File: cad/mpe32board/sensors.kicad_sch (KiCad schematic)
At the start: 93 parts, among them U4 TCA9548ARGER, U5 TCA9548ARGER, U6 TCA9548ARGER, U7 TCA9548ARGER, U8 TCA9548ARGER

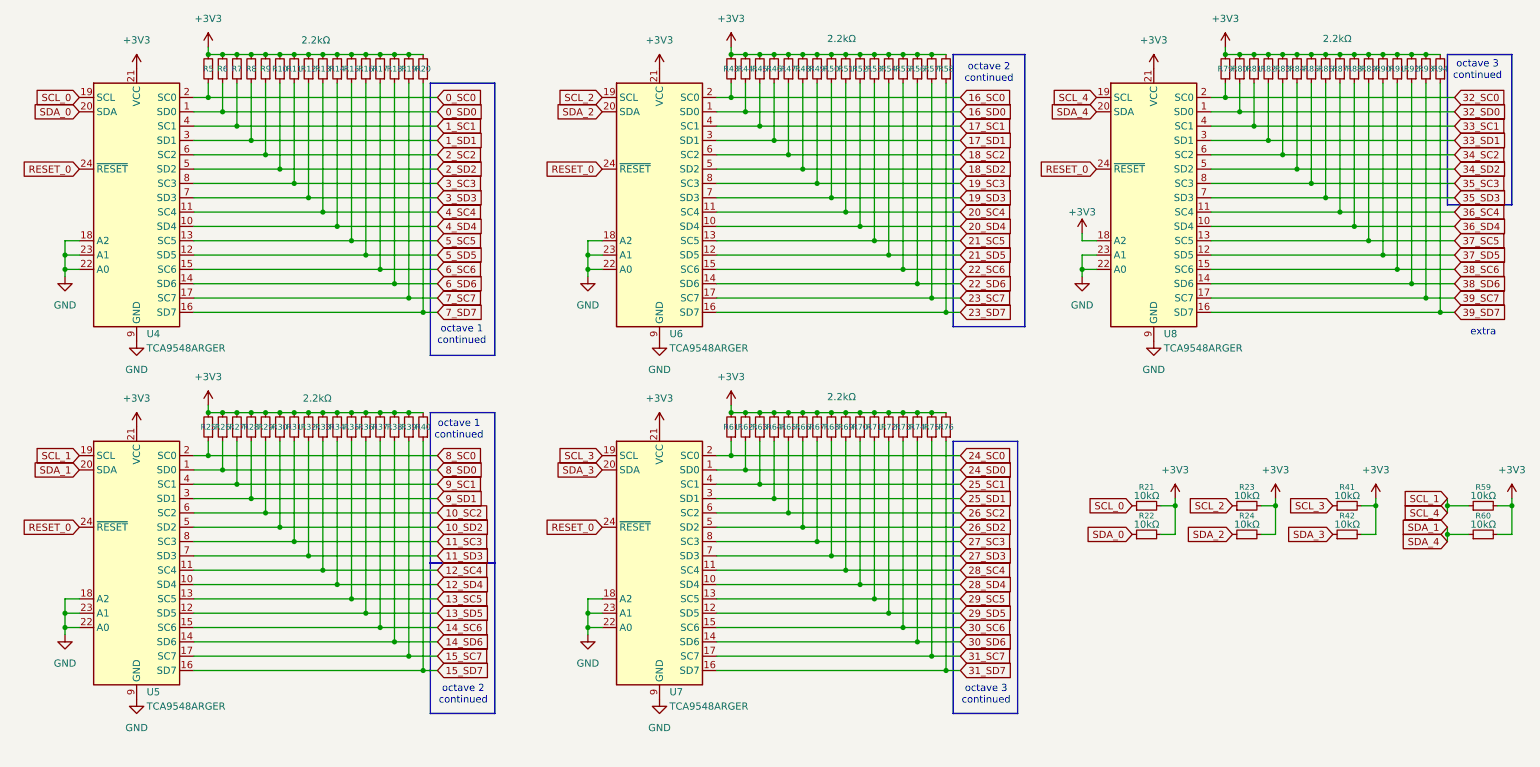
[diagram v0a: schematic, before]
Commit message: add sdram
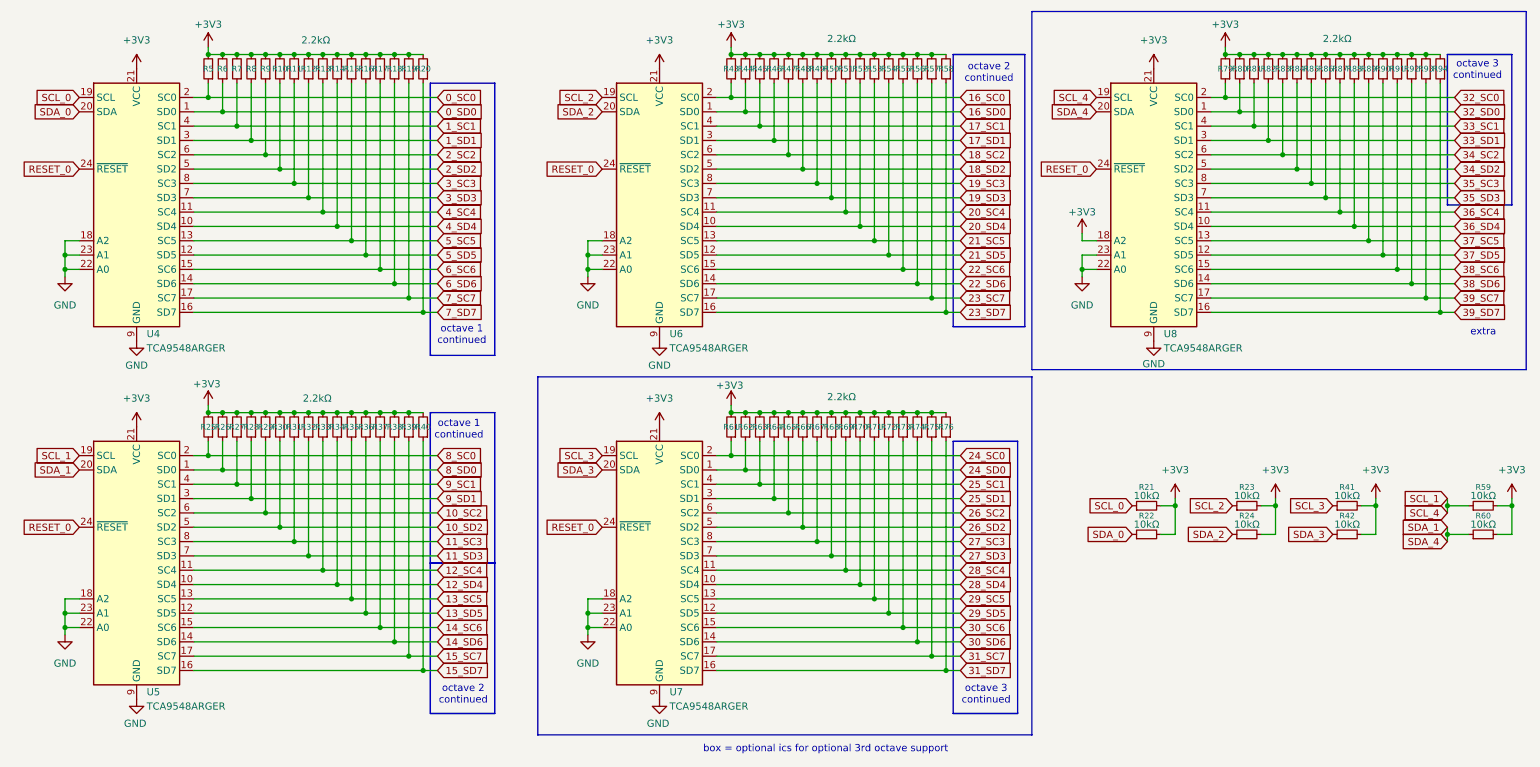
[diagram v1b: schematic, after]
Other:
- note added: "box = optional ics for optional 3rd octave support"
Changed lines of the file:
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@@
 	)
 	(rectangle
+		(start 106.68 81.28)
+		(end 194.31 144.78)
+		(stroke
+			(width 0)
+			(type default)
+		)
+		(fill
+			(type none)
+		)
+	)
+	(rectangle
 		(start 267.97 24.13)
 		(end 279.4 50.8)
@@
 		)
 	)
+	(rectangle
+		(start 194.31 16.51)
+		(end 281.94 80.01)
+		(stroke
+			(width 0)
+			(type default)
+		)
+		(fill
+			(type none)
+		)
+	)
 	(text "octave 3\ncontinued"
 		(exclude_from_sim no)
@@
 		)
 	)
+	(text "box = optional ics for optional 3rd octave support"
+		(exclude_from_sim no)
+		(at 157.734 147.32 0)
+		(effects
+			(font
+				(size 1.27 1.27)
+			)
+		)
+	)
 	(text "octave 2\ncontinued"
 		(exclude_from_sim no)
@@
 		(on_board yes)
 		(dnp no)
-		(fields_autoplaced yes)
 		(property "Reference" "#PWR037"
 			(at 48.26 26.67 0)
@@
 		)
 		(property "Value" "+3V3"
-			(at 48.26 17.78 0)
+			(at 48.26 18.796 0)
 			(effects
 				(font
@@
 		(on_board yes)
 		(dnp no)
-		(fields_autoplaced yes)
 		(property "Reference" "#PWR049"
 			(at 140.97 26.67 0)
@@
 		)
 		(property "Value" "+3V3"
-			(at 140.97 17.78 0)
+			(at 140.97 18.796 0)
 			(effects
 				(font
@@
 		(on_board yes)
 		(dnp no)
-		(fields_autoplaced yes)
 		(property "Reference" "#PWR048"
 			(at 128.27 81.28 0)
@@
 		)
 		(property "Value" "GND"
-			(at 128.27 80.01 0)
+			(at 128.27 79.248 0)
 			(effects
 				(font
@@
 		(on_board yes)
 		(dnp no)
-		(fields_autoplaced yes)
 		(property "Reference" "#PWR054"
 			(at 140.97 90.17 0)
@@
 		)
 		(property "Value" "+3V3"
-			(at 140.97 81.28 0)
+			(at 140.716 82.804 0)
 			(effects
 				(font
@@
 		(on_board yes)
 		(dnp no)
-		(fields_autoplaced yes)
 		(property "Reference" "#PWR053"
 			(at 128.27 144.78 0)
@@
 		)
 		(property "Value" "GND"
-			(at 128.27 143.51 0)
+			(at 128.016 142.748 0)
 			(effects
 				(font
@@
 		(on_board yes)
 		(dnp no)
-		(fields_autoplaced yes)
 		(property "Reference" "#PWR059"
 			(at 228.6 26.67 0)
@@
 		)
 		(property "Value" "+3V3"
-			(at 228.6 17.78 0)
+			(at 228.6 18.796 0)
 			(effects
 				(font
@@
 		(on_board yes)
 		(dnp no)
-		(fields_autoplaced yes)
 		(property "Reference" "#PWR044"
 			(at 48.26 90.17 0)
@@
 		)
 		(property "Value" "+3V3"
-			(at 48.26 81.28 0)
+			(at 48.006 82.55 0)
 			(effects
 				(font
@@
 		(on_board yes)
 		(dnp no)
-		(fields_autoplaced yes)
 		(property "Reference" "#PWR031"
 			(at 35.56 81.28 0)
@@
 		)
 		(property "Value" "GND"
-			(at 35.56 80.01 0)
+			(at 35.56 79.248 0)
 			(effects
 				(font
@@
 		(on_board yes)
 		(dnp no)
-		(fields_autoplaced yes)
 		(property "Reference" "#PWR043"
 			(at 35.56 144.78 0)
@@
 		)
 		(property "Value" "GND"
-			(at 35.56 143.51 0)
+			(at 35.306 142.748 0)
 			(effects
 				(font
@@
 		(on_board yes)
 		(dnp no)
-		(fields_autoplaced yes)
 		(property "Reference" "#PWR058"
 			(at 215.9 81.28 0)
@@
 		)
 		(property "Value" "GND"
-			(at 215.9 80.01 0)
+			(at 215.9 78.994 0)
 			(effects
 				(font
